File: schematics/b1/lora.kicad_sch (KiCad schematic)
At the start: 4 parts, among them U5 Ai-Thinker-Ra-02

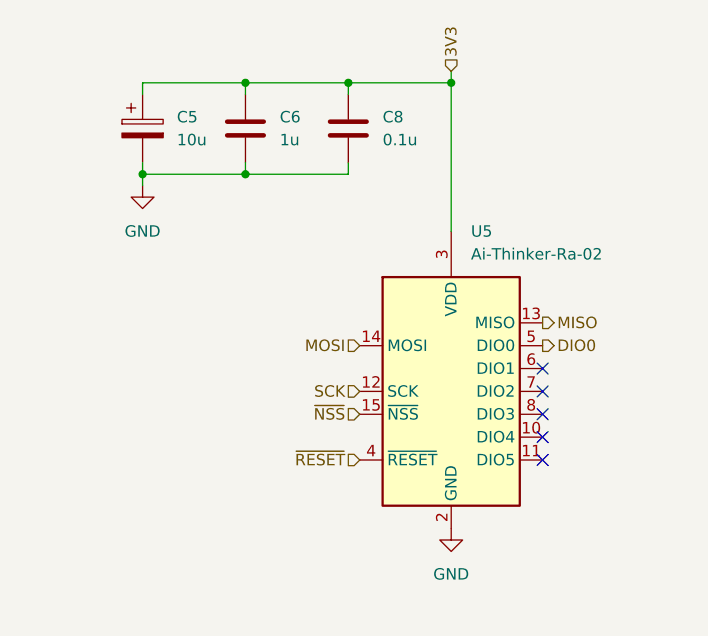
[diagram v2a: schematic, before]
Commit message: Added a bunch of test points.
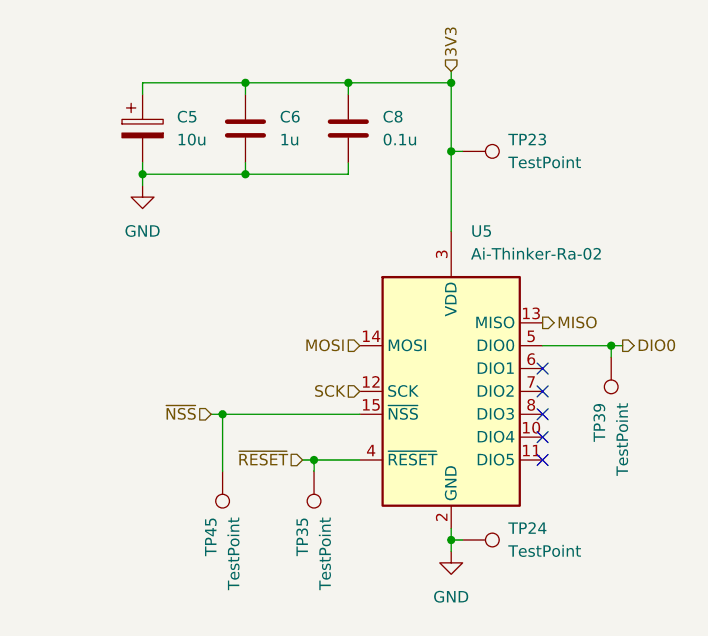
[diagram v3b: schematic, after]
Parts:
- added TP23, TP24, TP35, TP39, TP45: TestPoint, symbol Connector:TestPoint
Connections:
- net 3V3: now also TP23.1
- net DIO0: now also TP39.1
- net GND: now also TP24.1
- net ~{NSS}: now also TP45.1
- net ~{RESET}: now also TP35.1
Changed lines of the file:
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@@
     (comment 4 "The LoRa block is just an AI Thinker RA-02 LoRa module. This is used for backup")
   )
+  (junction (at 116.84 59.69) (diameter 0) (color 0 0 0 0)
+  )
   (junction (at 99.06 30.48) (diameter 0) (color 0 0 0 0)
   )
@@
   (junction (at 76.2 40.64) (diameter 0) (color 0 0 0 0)
   )
+  (junction (at 99.06 81.28) (diameter 0) (color 0 0 0 0)
+  )
+  (junction (at 99.06 38.1) (diameter 0) (color 0 0 0 0)
+  )
   (junction (at 87.63 30.48) (diameter 0) (color 0 0 0 0)
+  )
+  (junction (at 83.82 72.39) (diameter 0) (color 0 0 0 0)
+  )
+  (junction (at 73.66 67.31) (diameter 0) (color 0 0 0 0)
   )
   (junction (at 64.77 40.64) (diameter 0) (color 0 0 0 0)
@@
   (no_connect (at 109.22 64.77))
   (no_connect (at 109.22 69.85))
-  (wire (pts (xy 99.06 30.48) (xy 99.06 46.99))
+  (wire (pts (xy 99.06 30.48) (xy 99.06 38.1))
+    (stroke (width 0) (type default))
+  )
+  (wire (pts (xy 73.66 67.31) (xy 73.66 73.66))
+    (stroke (width 0) (type default))
+  )
+  (wire (pts (xy 72.39 67.31) (xy 73.66 67.31))
+    (stroke (width 0) (type default))
+  )
+  (wire (pts (xy 118.11 59.69) (xy 116.84 59.69))
     (stroke (width 0) (type default))
   )
@@
     (stroke (width 0) (type default))
   )
+  (wire (pts (xy 82.55 72.39) (xy 83.82 72.39))
+    (stroke (width 0) (type default))
+  )
+  (wire (pts (xy 99.06 81.28) (xy 99.06 80.01))
+    (stroke (width 0) (type default))
+  )
+  (wire (pts (xy 99.06 38.1) (xy 99.06 46.99))
+    (stroke (width 0) (type default))
+  )
+  (wire (pts (xy 109.22 59.69) (xy 116.84 59.69))
+    (stroke (width 0) (type default))
+  )
   (wire (pts (xy 64.77 41.91) (xy 64.77 40.64))
     (stroke (width 0) (type default))
   )
+  (wire (pts (xy 73.66 67.31) (xy 88.9 67.31))
+    (stroke (width 0) (type default))
+  )
+  (wire (pts (xy 99.06 81.28) (xy 100.33 81.28))
+    (stroke (width 0) (type default))
+  )
+  (wire (pts (xy 99.06 82.55) (xy 99.06 81.28))
+    (stroke (width 0) (type default))
+  )
   (wire (pts (xy 99.06 30.48) (xy 87.63 30.48))
     (stroke (width 0) (type default))
@@
     (stroke (width 0) (type default))
   )
+  (wire (pts (xy 83.82 72.39) (xy 88.9 72.39))
+    (stroke (width 0) (type default))
+  )
+  (wire (pts (xy 116.84 59.69) (xy 116.84 60.96))
+    (stroke (width 0) (type default))
+  )
   (wire (pts (xy 64.77 40.64) (xy 76.2 40.64))
     (stroke (width 0) (type default))
@@
     (stroke (width 0) (type default))
   )
+  (wire (pts (xy 99.06 38.1) (xy 100.33 38.1))
+    (stroke (width 0) (type default))
+  )
   (wire (pts (xy 87.63 30.48) (xy 87.63 31.75))
     (stroke (width 0) (type default))
   )
+  (wire (pts (xy 83.82 72.39) (xy 83.82 73.66))
+    (stroke (width 0) (type default))
+  )
   (wire (pts (xy 76.2 30.48) (xy 76.2 31.75))
     (stroke (width 0) (type default))
   )
-  (hierarchical_label "~{RESET}" (shape input) (at 88.9 72.39 180) (fields_autoplaced)
+  (hierarchical_label "~{RESET}" (shape input) (at 82.55 72.39 180) (fields_autoplaced)
     (effects (font (size 1.27 1.27)) (justify right))
   )
@@
     (effects (font (size 1.27 1.27)) (justify right))
   )
-  (hierarchical_label "~{NSS}" (shape input) (at 88.9 67.31 180) (fields_autoplaced)
+  (hierarchical_label "~{NSS}" (shape input) (at 72.39 67.31 180) (fields_autoplaced)
     (effects (font (size 1.27 1.27)) (justify right))
   )
-  (hierarchical_label "DIO0" (shape output) (at 109.22 59.69 0) (fields_autoplaced)
+  (hierarchical_label "DIO0" (shape output) (at 118.11 59.69 0) (fields_autoplaced)
     (effects (font (size 1.27 1.27)) (justify left))
   )
@@
     (effects (font (size 1.27 1.27)) (justify left))
   )
-  (symbol (lib_id "power:GND") (at 99.06 80.01 0) (unit 1)
-    (in_bom yes) (on_board yes) (dnp no) (fields_autoplaced)
-    (property "Reference" "#PWR020" (at 99.06 86.36 0)
-      (effects (font (size 1.27 1.27)) hide)
-    )
-    (property "Value" "GND" (at 99.06 85.09 0)
+  (symbol (lib_id "power:GND") (at 99.06 82.55 0) (unit 1)
+    (in_bom yes) (on_board yes) (dnp no) (fields_autoplaced)
+    (property "Reference" "#PWR020" (at 99.06 88.9 0)
+      (effects (font (size 1.27 1.27)) hide)
+    )
+    (property "Value" "GND" (at 99.06 87.63 0)
       (effects (font (size 1.27 1.27)))
     )
-    (property "Footprint" "" (at 99.06 80.01 0)
-      (effects (font (size 1.27 1.27)) hide)
-    )
-    (property "Datasheet" "" (at 99.06 80.01 0)
+    (property "Footprint" "" (at 99.06 82.55 0)
+      (effects (font (size 1.27 1.27)) hide)
+    )
+    (property "Datasheet" "" (at 99.06 82.55 0)
       (effects (font (size 1.27 1.27)) hide)
     )
@@
         (path "/d6142fa5-2354-4512-9919-37616259c364/bca829a9-1cbe-4403-a4e4-7724b6c8becd"
           (reference "#PWR020") (unit 1)
+        )
+      )
+    )
+  )
+  (symbol (lib_id "Connector:TestPoint") (at 100.33 38.1 270) (unit 1)
+    (in_bom yes) (on_board yes) (dnp no) (fields_autoplaced)
+    (property "Reference" "TP23" (at 105.41 36.83 90)
+      (effects (font (size 1.27 1.27)) (justify left))
+    )
+    (property "Value" "TestPoint" (at 105.41 39.37 90)
+      (effects (font (size 1.27 1.27)) (justify left))
+    )
+    (property "Footprint" "" (at 100.33 43.18 0)
+      (effects (font (size 1.27 1.27)) hide)
+    )
+    (property "Datasheet" "~" (at 100.33 43.18 0)
+      (effects (font (size 1.27 1.27)) hide)
+    )
+    (pin "1")
+    (instances
+      (project "b1"
+        (path "/d6142fa5-2354-4512-9919-37616259c364/bca829a9-1cbe-4403-a4e4-7724b6c8becd"
+          (reference "TP23") (unit 1)
         )
       )
@@
         (path "/d6142fa5-2354-4512-9919-37616259c364/bca829a9-1cbe-4403-a4e4-7724b6c8becd"
           (reference "C8") (unit 1)
+        )
+      )
+    )
+  )
+  (symbol (lib_id "Connector:TestPoint") (at 116.84 60.96 180) (unit 1)
+    (in_bom yes) (on_board yes) (dnp no)
+    (property "Reference" "TP39" (at 115.57 66.04 90)
+      (effects (font (size 1.27 1.27)) (justify left))
+    )
+    (property "Value" "TestPoint" (at 118.11 66.04 90)
+      (effects (font (size 1.27 1.27)) (justify left))
+    )
+    (property "Footprint" "" (at 111.76 60.96 0)
+      (effects (font (size 1.27 1.27)) hide)
+    )
+    (property "Datasheet" "~" (at 111.76 60.96 0)
+      (effects (font (size 1.27 1.27)) hide)
+    )
+    (pin "1")
+    (instances
+      (project "b1"
+        (path "/d6142fa5-2354-4512-9919-37616259c364/bca829a9-1cbe-4403-a4e4-7724b6c8becd"
+          (reference "TP39") (unit 1)
         )
       )
@@
     )
   )
+  (symbol (lib_id "Connector:TestPoint") (at 83.82 73.66 180) (unit 1)
+    (in_bom yes) (on_board yes) (dnp no)
+    (property "Reference" "TP35" (at 82.55 78.74 90)
+      (effects (font (size 1.27 1.27)) (justify left))
+    )
+    (property "Value" "TestPoint" (at 85.09 78.74 90)
+      (effects (font (size 1.27 1.27)) (justify left))
+    )
+    (property "Footprint" "" (at 78.74 73.66 0)
+      (effects (font (size 1.27 1.27)) hide)
+    )
+    (property "Datasheet" "~" (at 78.74 73.66 0)
+      (effects (font (size 1.27 1.27)) hide)
+    )
+    (pin "1")
+    (instances
+      (project "b1"
+        (path "/d6142fa5-2354-4512-9919-37616259c364/bca829a9-1cbe-4403-a4e4-7724b6c8becd"
+          (reference "TP35") (unit 1)
+        )
+      )
+    )
+  )
   (symbol (lib_id "Device:C") (at 76.2 35.56 0) (unit 1)
     (in_bom yes) (on_board yes) (dnp no) (fields_autoplaced)
@@
         (path "/d6142fa5-2354-4512-9919-37616259c364/bca829a9-1cbe-4403-a4e4-7724b6c8becd"
           (reference "C6") (unit 1)
+        )
+      )
+    )
+  )
+  (symbol (lib_id "Connector:TestPoint") (at 100.33 81.28 270) (unit 1)
+    (in_bom yes) (on_board yes) (dnp no) (fields_autoplaced)
+    (property "Reference" "TP24" (at 105.41 80.01 90)
+      (effects (font (size 1.27 1.27)) (justify left))
+    )
+    (property "Value" "TestPoint" (at 105.41 82.55 90)
+      (effects (font (size 1.27 1.27)) (justify left))
+    )
+    (property "Footprint" "" (at 100.33 86.36 0)
+      (effects (font (size 1.27 1.27)) hide)
+    )
+    (property "Datasheet" "~" (at 100.33 86.36 0)
+      (effects (font (size 1.27 1.27)) hide)
+    )
+    (pin "1")
+    (instances
+      (project "b1"
+        (path "/d6142fa5-2354-4512-9919-37616259c364/bca829a9-1cbe-4403-a4e4-7724b6c8becd"
+          (reference "TP24") (unit 1)
         )
       )
@@
         )
       )
+    )
+  )
+  (symbol (lib_id "Connector:TestPoint") (at 73.66 73.66 180) (unit 1)
+    (in_bom yes) (on_board yes) (dnp no)
+    (property "Reference" "TP45" (at 72.39 78.74 90)
+      (effects (font (size 1.27 1.27)) (justify left))
+    )
+    (property "Value" "TestPoint" (at 74.93 78.74 90)
+      (effects (font (size 1.27 1.27)) (justify left))
+    )
+    (property "Footprint" "" (at 68.58 73.66 0)
+      (effects (font (size 1.27 1.27)) hide)
+    )
+    (property "Datasheet" "~" (at 68.58 73.66 0)
+      (effects (font (size 1.27 1.27)) hide)
+    )
+    (pin "1")
+    (instances
+      (project "b1"
+        (path "/d6142fa5-2354-4512-9919-37616259c364/bca829a9-1cbe-4403-a4e4-7724b6c8becd"
+          (reference "TP45") (unit 1)
+        )
+      )

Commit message: Added a big bulk cap to the LoRa module.
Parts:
- added C29: 1m, symbol Device:C_Polarized
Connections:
- net 3V3: now also C29.1
- net GND: now also C29.2
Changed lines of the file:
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@@
   (junction (at 99.06 30.48) (diameter 0) (color 0 0 0 0)
   )
+  (junction (at 53.34 40.64) (diameter 0) (color 0 0 0 0)
+  )
   (junction (at 76.2 30.48) (diameter 0) (color 0 0 0 0)
   )
@@
   )
   (junction (at 64.77 40.64) (diameter 0) (color 0 0 0 0)
+  )
+  (junction (at 64.77 30.48) (diameter 0) (color 0 0 0 0)
   )
   (no_connect (at 109.22 72.39))
@@
     (stroke (width 0) (type default))
   )
+  (wire (pts (xy 53.34 31.75) (xy 53.34 30.48))
+    (stroke (width 0) (type default))
+  )
   (wire (pts (xy 87.63 30.48) (xy 76.2 30.48))
     (stroke (width 0) (type default))
@@
     (stroke (width 0) (type default))
   )
+  (wire (pts (xy 53.34 39.37) (xy 53.34 40.64))
+    (stroke (width 0) (type default))
+  )
   (wire (pts (xy 99.06 38.1) (xy 99.06 46.99))
     (stroke (width 0) (type default))
@@
     (stroke (width 0) (type default))
   )
-  (wire (pts (xy 64.77 41.91) (xy 64.77 40.64))
+  (wire (pts (xy 53.34 41.91) (xy 53.34 40.64))
     (stroke (width 0) (type default))
   )
@@
   )
   (wire (pts (xy 76.2 40.64) (xy 87.63 40.64))
+    (stroke (width 0) (type default))
+  )
+  (wire (pts (xy 53.34 30.48) (xy 64.77 30.48))
+    (stroke (width 0) (type default))
+  )
+  (wire (pts (xy 53.34 40.64) (xy 64.77 40.64))
     (stroke (width 0) (type default))
   )
@@
     )
   )
+  (symbol (lib_id "Device:C_Polarized") (at 53.34 35.56 0) (unit 1)
+    (in_bom yes) (on_board yes) (dnp no)
+    (property "Reference" "C29" (at 57.15 34.29 0)
+      (effects (font (size 1.27 1.27)) (justify left))
+    )
+    (property "Value" "1m" (at 57.15 36.83 0)
+      (effects (font (size 1.27 1.27)) (justify left))
+    )
+    (property "Footprint" "" (at 54.3052 39.37 0)
+      (effects (font (size 1.27 1.27)) hide)
+    )
+    (property "Datasheet" "~" (at 53.34 35.56 0)
+      (effects (font (size 1.27 1.27)) hide)
+    )
+    (pin "2")
+    (pin "1")
+    (instances
+      (project "b1"
+        (path "/d6142fa5-2354-4512-9919-37616259c364/bca829a9-1cbe-4403-a4e4-7724b6c8becd"
+          (reference "C29") (unit 1)
+        )
+      )
+    )
+  )
   (symbol (lib_id "Connector:TestPoint") (at 100.33 81.28 270) (unit 1)
     (in_bom yes) (on_board yes) (dnp no) (fields_autoplaced)
@@
     )
   )
-  (symbol (lib_id "power:GND") (at 64.77 41.91 0) (unit 1)
-    (in_bom yes) (on_board yes) (dnp no) (fields_autoplaced)
-    (property "Reference" "#PWR010" (at 64.77 48.26 0)
-      (effects (font (size 1.27 1.27)) hide)
-    )
-    (property "Value" "GND" (at 64.77 46.99 0)
+  (symbol (lib_id "power:GND") (at 53.34 41.91 0) (unit 1)
+    (in_bom yes) (on_board yes) (dnp no) (fields_autoplaced)
+    (property "Reference" "#PWR010" (at 53.34 48.26 0)
+      (effects (font (size 1.27 1.27)) hide)
+    )
+    (property "Value" "GND" (at 53.34 46.99 0)
       (effects (font (size 1.27 1.27)))
     )
-    (property "Footprint" "" (at 64.77 41.91 0)
-      (effects (font (size 1.27 1.27)) hide)
-    )
-    (property "Datasheet" "" (at 64.77 41.91 0)
-      (effects (font (size 1.27 1.27)) hide)
-    )
+    (property "Footprint" "" (at 53.34 41.91 0)
+      (effects (font (size 1.27 1.27)) hide)
+    )
+    (property "Datasheet" "" (at 53.34 41.91 0)
+      (effects (font (size 1.27 1.27)) hide)
+    )

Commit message: Updated annotations.
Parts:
- renumbered C29 to C26, C5 to C27, C6 to C28, C8 to C29, TP23 to TP41, TP39 to TP42, TP45 to TP43, TP35 to TP44, TP24 to TP45, U5 to U7
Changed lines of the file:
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@@
   (symbol (lib_id "power:GND") (at 99.06 82.55 0) (unit 1)
     (in_bom yes) (on_board yes) (dnp no) (fields_autoplaced)
-    (property "Reference" "#PWR020" (at 99.06 88.9 0)
+    (property "Reference" "#PWR038" (at 99.06 88.9 0)
       (effects (font (size 1.27 1.27)) hide)
     )
@@
       (project "b1"
         (path "/d6142fa5-2354-4512-9919-37616259c364/bca829a9-1cbe-4403-a4e4-7724b6c8becd"
-          (reference "#PWR020") (unit 1)
+          (reference "#PWR038") (unit 1)
         )
       )
@@
   )
   (symbol (lib_id "Connector:TestPoint") (at 100.33 38.1 270) (unit 1)
-    (in_bom yes) (on_board yes) (dnp no) (fields_autoplaced)
-    (property "Reference" "TP23" (at 105.41 36.83 90)
+    (in_bom yes) (on_board yes) (dnp no)
+    (property "Reference" "TP41" (at 105.41 38.1 90)
       (effects (font (size 1.27 1.27)) (justify left))
     )
     (property "Value" "TestPoint" (at 105.41 39.37 90)
-      (effects (font (size 1.27 1.27)) (justify left))
+      (effects (font (size 1.27 1.27)) (justify left) hide)
     )
     (property "Footprint" "" (at 100.33 43.18 0)
@@
       (project "b1"
         (path "/d6142fa5-2354-4512-9919-37616259c364/bca829a9-1cbe-4403-a4e4-7724b6c8becd"
-          (reference "TP23") (unit 1)
+          (reference "TP41") (unit 1)
         )
       )
@@
   (symbol (lib_id "Device:C") (at 87.63 35.56 0) (unit 1)
     (in_bom yes) (on_board yes) (dnp no)
-    (property "Reference" "C8" (at 91.44 34.29 0)
+    (property "Reference" "C29" (at 91.44 34.29 0)
       (effects (font (size 1.27 1.27)) (justify left))
     )
@@
       (project "b1"
         (path "/d6142fa5-2354-4512-9919-37616259c364/bca829a9-1cbe-4403-a4e4-7724b6c8becd"
-          (reference "C8") (unit 1)
+          (reference "C29") (unit 1)
         )
       )
@@
   (symbol (lib_id "Connector:TestPoint") (at 116.84 60.96 180) (unit 1)
     (in_bom yes) (on_board yes) (dnp no)
-    (property "Reference" "TP39" (at 115.57 66.04 90)
+    (property "Reference" "TP42" (at 116.84 66.04 90)
       (effects (font (size 1.27 1.27)) (justify left))
     )
     (property "Value" "TestPoint" (at 118.11 66.04 90)
-      (effects (font (size 1.27 1.27)) (justify left))
+      (effects (font (size 1.27 1.27)) (justify left) hide)
     )
     (property "Footprint" "" (at 111.76 60.96 0)
@@
       (project "b1"
         (path "/d6142fa5-2354-4512-9919-37616259c364/bca829a9-1cbe-4403-a4e4-7724b6c8becd"
-          (reference "TP39") (unit 1)
+          (reference "TP42") (unit 1)
         )
       )
@@
   (symbol (lib_id "RF_Module:Ai-Thinker-Ra-02") (at 99.06 64.77 0) (unit 1)
     (in_bom yes) (on_board yes) (dnp no) (fields_autoplaced)
-    (property "Reference" "U5" (at 101.2541 46.99 0)
+    (property "Reference" "U7" (at 101.2541 46.99 0)
       (effects (font (size 1.27 1.27)) (justify left))
     )
@@
       (project "b1"
         (path "/d6142fa5-2354-4512-9919-37616259c364/bca829a9-1cbe-4403-a4e4-7724b6c8becd"
-          (reference "U5") (unit 1)
+          (reference "U7") (unit 1)
         )
       )
@@
   (symbol (lib_id "Connector:TestPoint") (at 83.82 73.66 180) (unit 1)
     (in_bom yes) (on_board yes) (dnp no)
-    (property "Reference" "TP35" (at 82.55 78.74 90)
+    (property "Reference" "TP44" (at 83.82 78.74 90)
       (effects (font (size 1.27 1.27)) (justify left))
     )
     (property "Value" "TestPoint" (at 85.09 78.74 90)
-      (effects (font (size 1.27 1.27)) (justify left))
+      (effects (font (size 1.27 1.27)) (justify left) hide)
     )
     (property "Footprint" "" (at 78.74 73.66 0)
@@
       (project "b1"
         (path "/d6142fa5-2354-4512-9919-37616259c364/bca829a9-1cbe-4403-a4e4-7724b6c8becd"
-          (reference "TP35") (unit 1)
+          (reference "TP44") (unit 1)
         )
       )
@@
   (symbol (lib_id "Device:C") (at 76.2 35.56 0) (unit 1)
     (in_bom yes) (on_board yes) (dnp no) (fields_autoplaced)
-    (property "Reference" "C6" (at 80.01 34.29 0)
+    (property "Reference" "C28" (at 80.01 34.29 0)
       (effects (font (size 1.27 1.27)) (justify left))
     )
@@
       (project "b1"
         (path "/d6142fa5-2354-4512-9919-37616259c364/bca829a9-1cbe-4403-a4e4-7724b6c8becd"
-          (reference "C6") (unit 1)
+          (reference "C28") (unit 1)
         )
       )
@@
   (symbol (lib_id "Device:C_Polarized") (at 53.34 35.56 0) (unit 1)
     (in_bom yes) (on_board yes) (dnp no)
-    (property "Reference" "C29" (at 57.15 34.29 0)
+    (property "Reference" "C26" (at 57.15 34.29 0)
       (effects (font (size 1.27 1.27)) (justify left))
     )
@@
       (project "b1"
         (path "/d6142fa5-2354-4512-9919-37616259c364/bca829a9-1cbe-4403-a4e4-7724b6c8becd"
-          (reference "C29") (unit 1)
+          (reference "C26") (unit 1)
         )
       )
@@
   )
   (symbol (lib_id "Connector:TestPoint") (at 100.33 81.28 270) (unit 1)
-    (in_bom yes) (on_board yes) (dnp no) (fields_autoplaced)
-    (property "Reference" "TP24" (at 105.41 80.01 90)
+    (in_bom yes) (on_board yes) (dnp no)
+    (property "Reference" "TP45" (at 105.41 81.28 90)
       (effects (font (size 1.27 1.27)) (justify left))
     )
     (property "Value" "TestPoint" (at 105.41 82.55 90)
-      (effects (font (size 1.27 1.27)) (justify left))
+      (effects (font (size 1.27 1.27)) (justify left) hide)
     )
     (property "Footprint" "" (at 100.33 86.36 0)
@@
       (project "b1"
         (path "/d6142fa5-2354-4512-9919-37616259c364/bca829a9-1cbe-4403-a4e4-7724b6c8becd"
-          (reference "TP24") (unit 1)
+          (reference "TP45") (unit 1)
         )
       )
@@
   (symbol (lib_id "Device:C_Polarized") (at 64.77 35.56 0) (unit 1)
     (in_bom yes) (on_board yes) (dnp no)
-    (property "Reference" "C5" (at 68.58 34.29 0)
+    (property "Reference" "C27" (at 68.58 34.29 0)
       (effects (font (size 1.27 1.27)) (justify left))
     )
@@
       (project "b1"
         (path "/d6142fa5-2354-4512-9919-37616259c364/bca829a9-1cbe-4403-a4e4-7724b6c8becd"
-          (reference "C5") (unit 1)
+          (reference "C27") (unit 1)
         )
       )
@@
   (symbol (lib_id "power:GND") (at 53.34 41.91 0) (unit 1)
     (in_bom yes) (on_board yes) (dnp no) (fields_autoplaced)
-    (property "Reference" "#PWR010" (at 53.34 48.26 0)
+    (property "Reference" "#PWR037" (at 53.34 48.26 0)
       (effects (font (size 1.27 1.27)) hide)
     )
@@
       (project "b1"
         (path "/d6142fa5-2354-4512-9919-37616259c364/bca829a9-1cbe-4403-a4e4-7724b6c8becd"
-          (reference "#PWR010") (unit 1)
+          (reference "#PWR037") (unit 1)
         )
       )
@@
   (symbol (lib_id "Connector:TestPoint") (at 73.66 73.66 180) (unit 1)
     (in_bom yes) (on_board yes) (dnp no)
-    (property "Reference" "TP45" (at 72.39 78.74 90)
+    (property "Reference" "TP43" (at 73.66 78.74 90)
       (effects (font (size 1.27 1.27)) (justify left))
     )
     (property "Value" "TestPoint" (at 74.93 78.74 90)
-      (effects (font (size 1.27 1.27)) (justify left))
+      (effects (font (size 1.27 1.27)) (justify left) hide)
     )
     (property "Footprint" "" (at 68.58 73.66 0)
@@
       (project "b1"
         (path "/d6142fa5-2354-4512-9919-37616259c364/bca829a9-1cbe-4403-a4e4-7724b6c8becd"
-          (reference "TP45") (unit 1)
-        )
-      )
+          (reference "TP43") (unit 1)
+        )
+      )
